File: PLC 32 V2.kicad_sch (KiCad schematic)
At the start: 5 parts

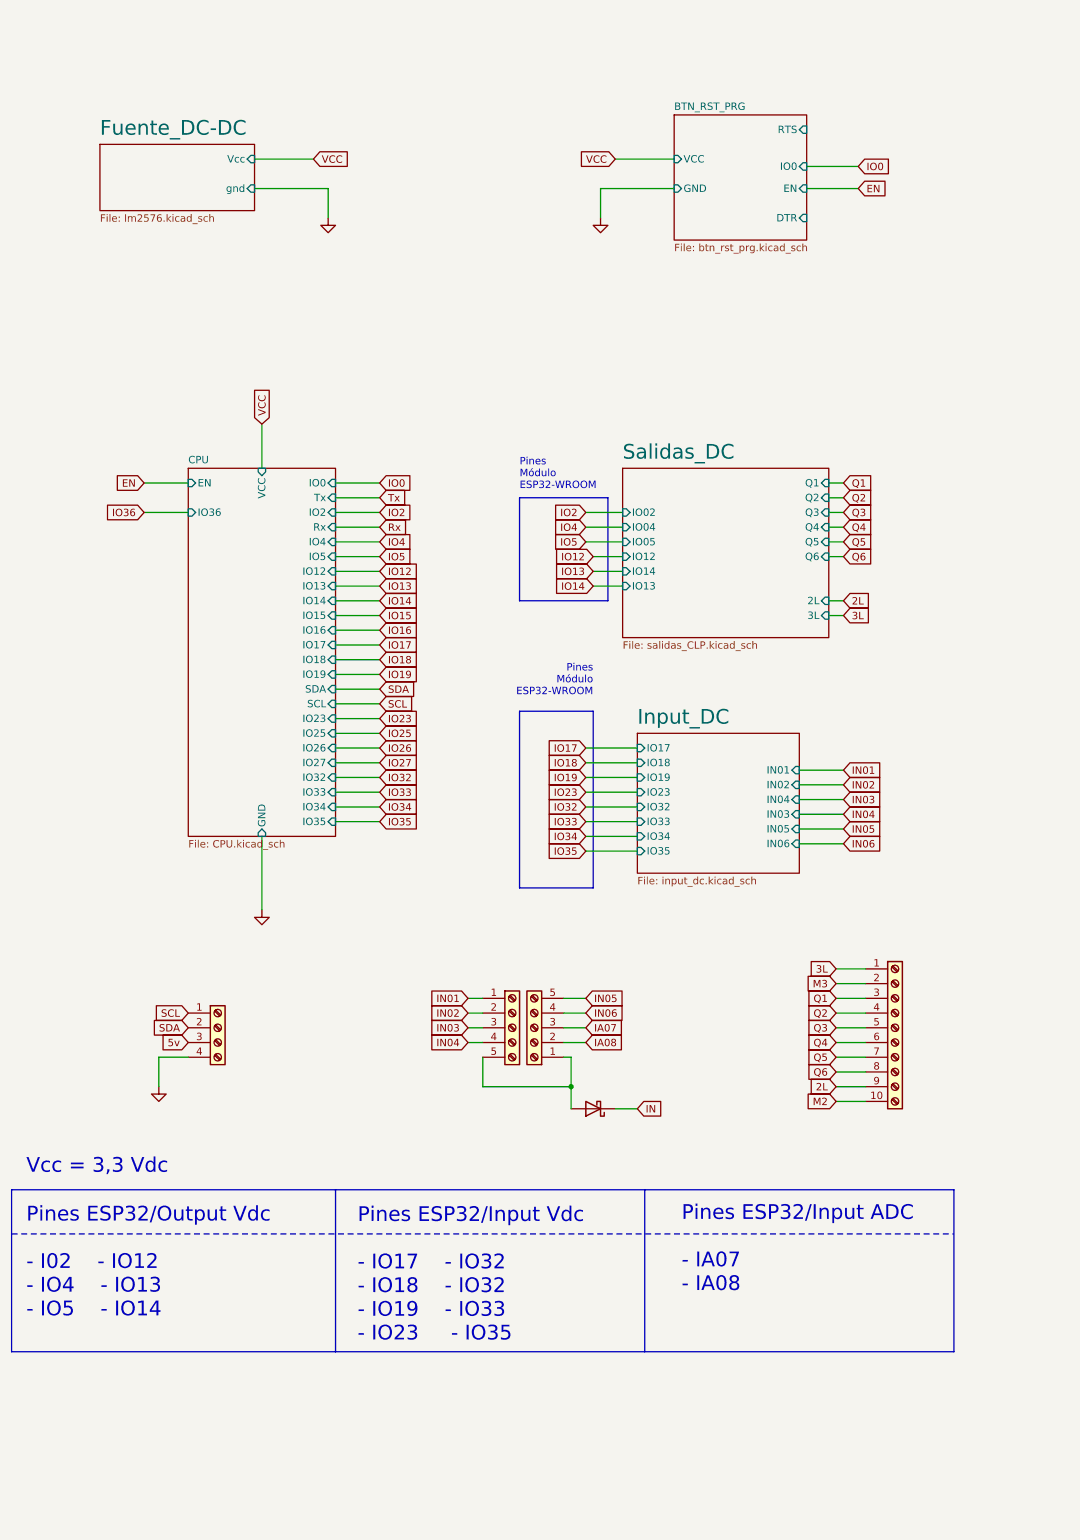
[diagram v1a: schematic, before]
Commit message: add entradas separadas
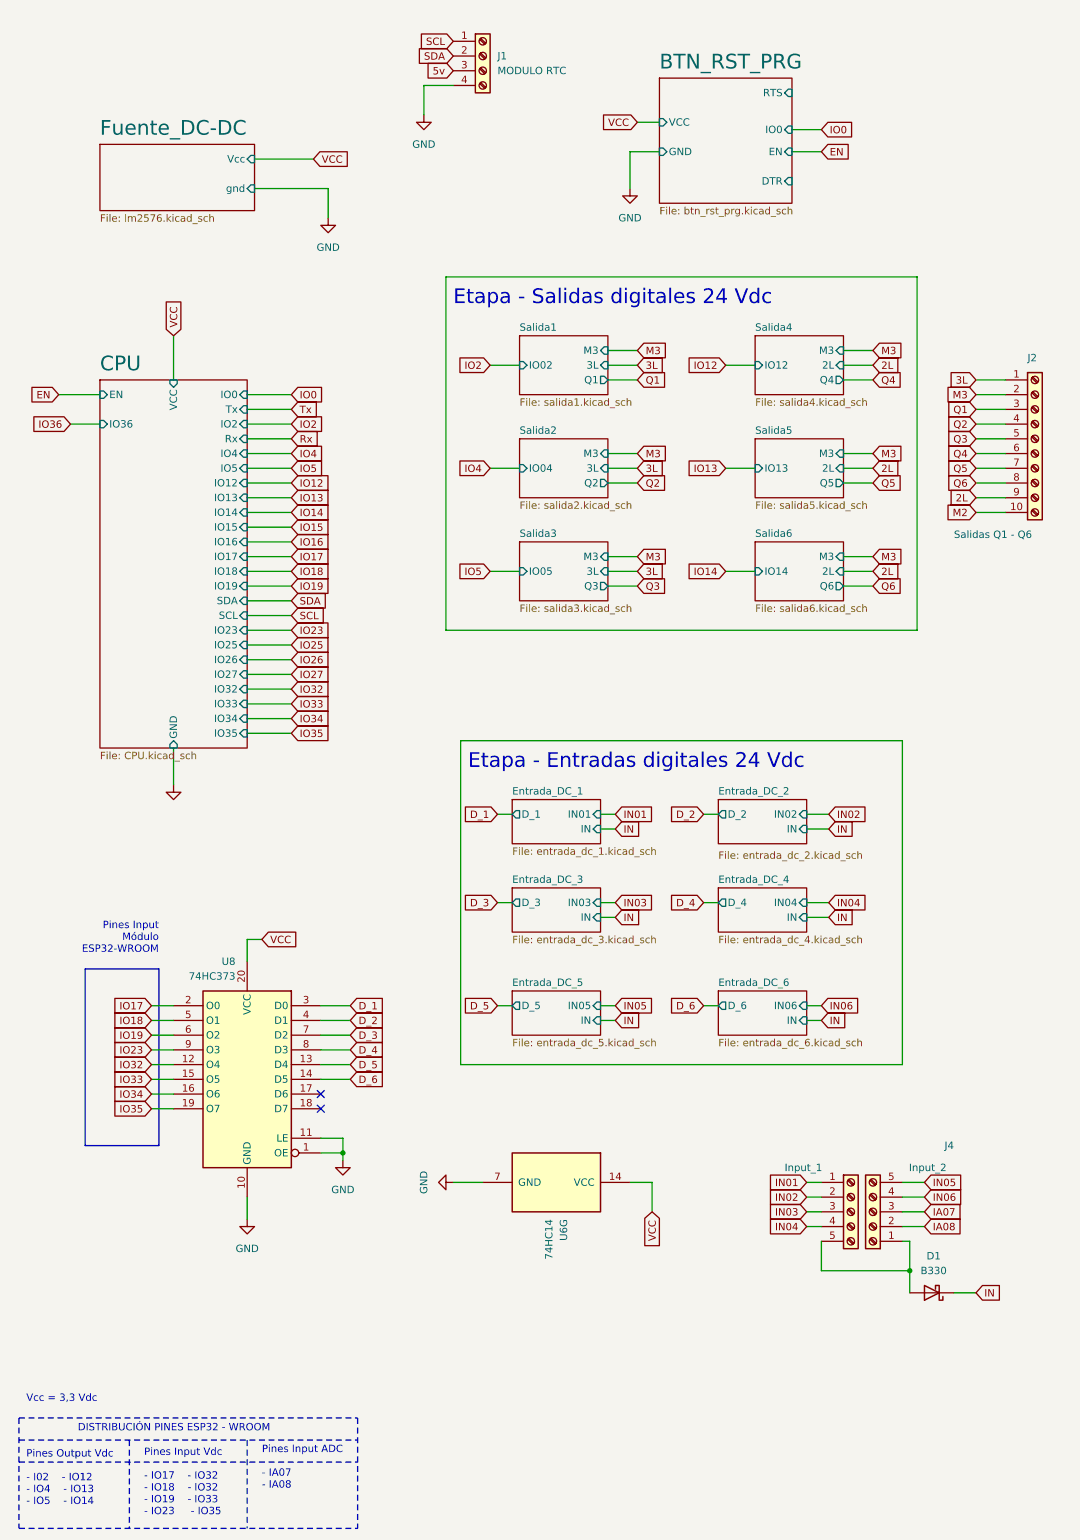
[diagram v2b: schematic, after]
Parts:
- removed ?: (no value), symbol Connector:Screw_Terminal_01x10
- removed ?: (no value), symbol Connector:Screw_Terminal_01x04
- added J1: MODULO RTC, Connector_PinHeader_2.54mm:PinHeader_1x04_P2.54mm_Vertical, symbol Connector:Screw_Terminal_01x04
- added J2: Salidas Q1 - Q6, TerminalBlock_Phoenix:TerminalBlock_Phoenix_PT-1,5-10-5.0-H_1x10_P5.00mm_Horizontal, symbol Connector:Screw_Terminal_01x10
- added U6: 74HC14, Package_SO:SOIC-14W_7.5x9mm_P1.27mm, symbol 74xx:74HC14
- added U8: 74HC373, Package_SO:SSOP-20_4.4x6.5mm_P0.65mm, symbol 74xx:74HC373
- D1: renamed from ?; value (none) -> B330; footprint (none) -> Diode_SMD:D_0402_1005Metric
- J3: renamed from ?; value (none) -> Input_1; footprint (none) -> TerminalBlock:TerminalBlock_bornier-5_P5.08mm
- J4: renamed from ?; value (none) -> Input_2; footprint (none) -> TerminalBlock:TerminalBlock_bornier-5_P5.08mm
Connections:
- net 2L: now also J2.9 (Pin_9)
- net 3L: now also J2.1 (Pin_1)
- net 5v: now also J1.3 (Pin_3)
- net GND: now also J1.4 (Pin_4), U6.7 (GND), U8.1 (OE), U8.10 (GND), U8.11 (LE)
- net IO17: now also U8.2 (O0)
- net IO18: now also U8.5 (O1)
- net IO19: now also U8.6 (O2)
- net IO23: now also U8.9 (O3)
- net IO32: now also U8.12 (O4)
- net IO33: now also U8.15 (O5)
- net IO34: now also U8.16 (O6)
- net IO35: now also U8.19 (O7)
- net M2: now also J2.10 (Pin_10)
- net M3: now also J2.2 (Pin_2)
- net Q1: now also J2.3 (Pin_3)
- net Q2: now also J2.4 (Pin_4)
- net Q3: now also J2.5 (Pin_5)
- net Q4: now also J2.6 (Pin_6)
- net Q5: now also J2.7 (Pin_7)
- net Q6: now also J2.8 (Pin_8)
- net SCL: now also J1.1 (Pin_1)
- net SDA: now also J1.2 (Pin_2)
- net VCC: now also U6.14 (VCC), U8.20 (VCC)
- new net D_1: U8.3 (D0)
- new net D_2: U8.4 (D1)
- new net D_3: U8.7 (D2)
- new net D_4: U8.8 (D3)
- new net D_5: U8.13 (D4)
- new net D_6: U8.14 (D5)
- no-connect marks 0 -> 2
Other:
- removed sheet Input_DC
- removed sheet Salidas_DC
- added sheet Entrada_DC_1 (entrada_dc_1.kicad_sch)
- added sheet Entrada_DC_2 (entrada_dc_2.kicad_sch)
- added sheet Entrada_DC_3 (entrada_dc_3.kicad_sch)
- added sheet Entrada_DC_4 (entrada_dc_4.kicad_sch)
- added sheet Entrada_DC_5 (entrada_dc_5.kicad_sch)
- added sheet Entrada_DC_6 (entrada_dc_6.kicad_sch)
- added sheet Salida1 (salida1.kicad_sch)
- added sheet Salida2 (salida2.kicad_sch)
- added sheet Salida3 (salida3.kicad_sch)
- added sheet Salida4 (salida4.kicad_sch)
- added sheet Salida5 (salida5.kicad_sch)
- added sheet Salida6 (salida6.kicad_sch)
- note added: "DISTRIBUCIÓN PINES ESP32 - WROOM"
- note added: "Etapa - Entradas digitales 24 Vdc"
- note added: "Etapa - Salidas digitales 24 Vdc"
- note added: "Pines Input ADC - IA07 - IA08"
- note added: "Pines Input Módulo ESP32-WROOM"
- note added: "Pines Input Vdc - IO17 - IO32 - IO18 - IO32 - IO19 - IO33 - IO23 - IO35"
- note added: "Pines Output Vdc - I02 - IO12 - IO4 - IO13 - IO5 - IO14"
- note removed: "Pines ESP32/Input ADC - IA07 - IA08"
- note removed: "Pines ESP32/Input Vdc - IO17 - IO32 - IO18 - IO32 - IO19 - IO33 - IO23 - IO35"
- note removed: "Pines ESP32/Output Vdc - I02 - IO12 - IO4 - IO13 - IO5 - IO14"
- note removed: "Pines Módulo ESP32-WROOM"

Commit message: input/output separadas
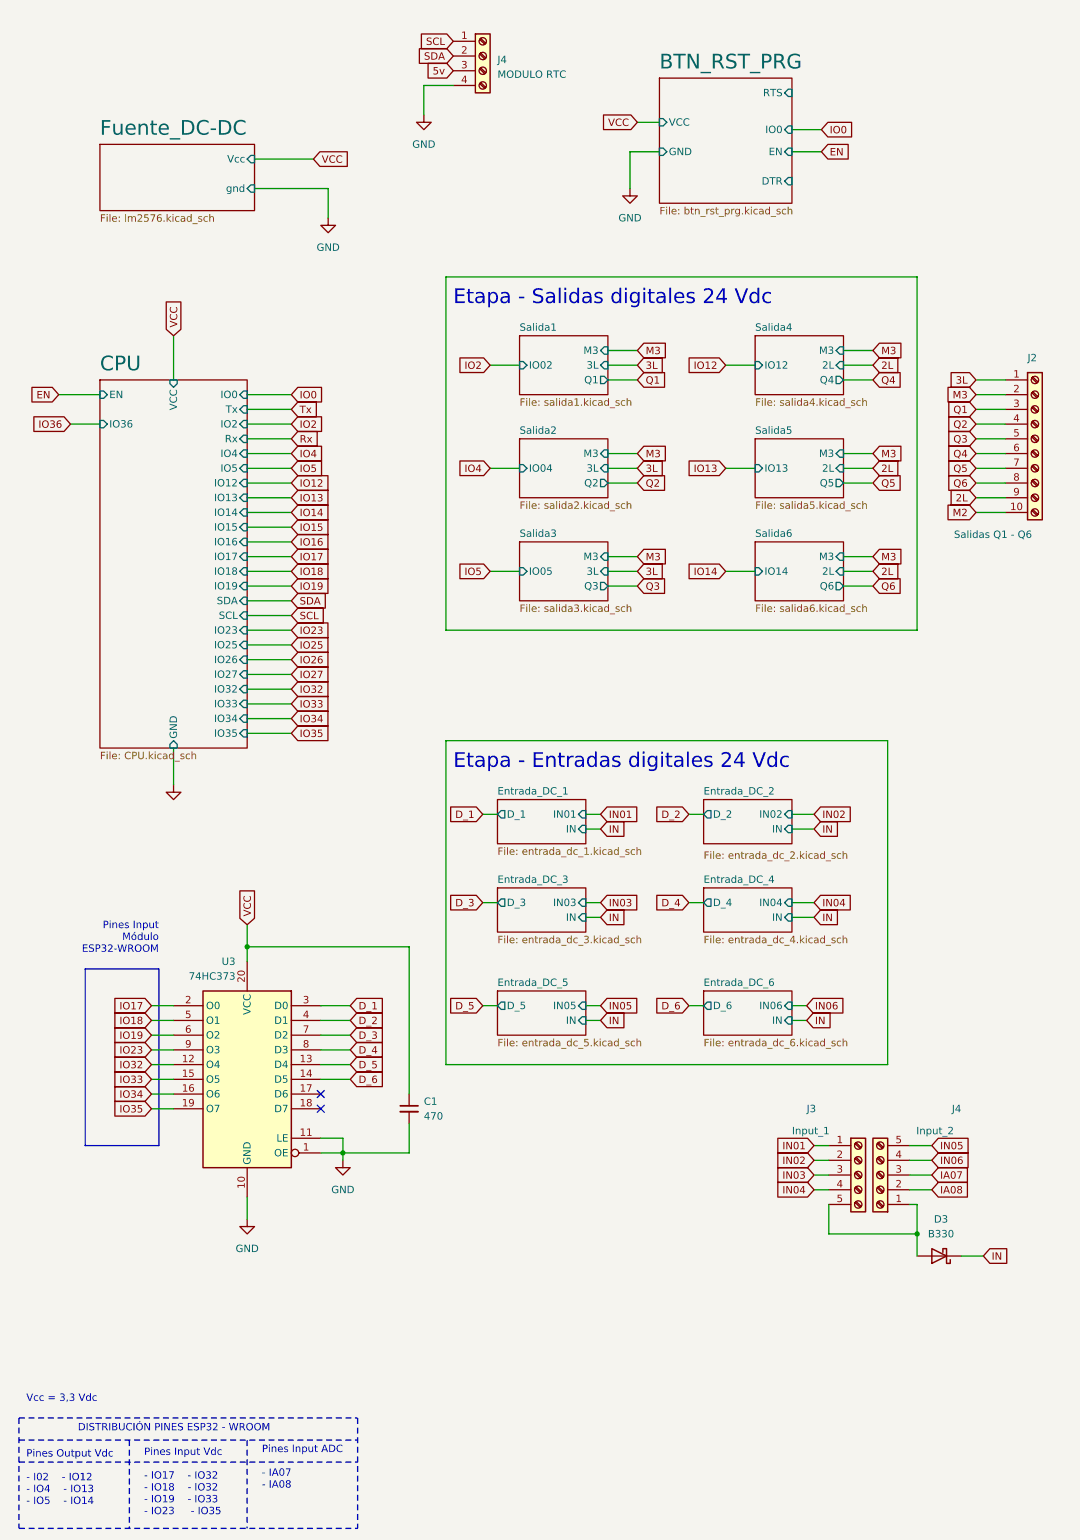
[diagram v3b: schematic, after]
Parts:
- removed U6: 74HC14, Package_SO:SOIC-14W_7.5x9mm_P1.27mm, symbol 74xx:74HC14
- added C1: 470, Capacitor_SMD:C_Elec_10x10.2, symbol Device:C_Small
- renumbered D1 to D3, J1 to J4, U8 to U3
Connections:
- net GND: now also C1.2
- net VCC: now also C1.1
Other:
- moved on the sheet: D3, J4

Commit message: add
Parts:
- removed J4: MODULO RTC, Connector_PinHeader_2.54mm:PinHeader_1x04_P2.54mm_Vertical, symbol Connector:Screw_Terminal_01x04
- renumbered D3 to D1, J3 to J2, J4 to J3, J2 to J4, U3 to U1
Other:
- sheet BTN_RST_PRG ports: added none; removed GND
- sheet Fuente_DC-DC ports: added GND, VCC; removed Vcc, gnd
- note removed: "Etapa - Entradas digitales 24 Vdc"
- note removed: "Etapa - Salidas digitales 24 Vdc"
